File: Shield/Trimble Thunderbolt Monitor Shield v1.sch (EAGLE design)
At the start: 32 parts, among them Q1 2N2222, U2 MAX232PTH

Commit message: Changed the pot used for LCD contrast to a 3362U package.
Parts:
- TRIMLCD: device SparkFun:POTTRIM -> SparkFun:POT100K_3362U
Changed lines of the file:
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@@
 <part name="GND4" library="supply1" deviceset="GND" device=""/>
 <part name="GND5" library="supply1" deviceset="GND" device=""/>
-<part name="TRIMLCD" library="SparkFun" deviceset="POT" device="TRIM" value="10K"/>
+<part name="TRIMLCD" library="SparkFun" deviceset="POT" device="100K_3362U" value="10K"/>
 <part name="R7" library="SparkFun" deviceset="RESISTOR" device="AXIAL-0.3" value="4.7K"/>
 <part name="R8" library="SparkFun" deviceset="RESISTOR" device="AXIAL-0.3" value="10K"/>

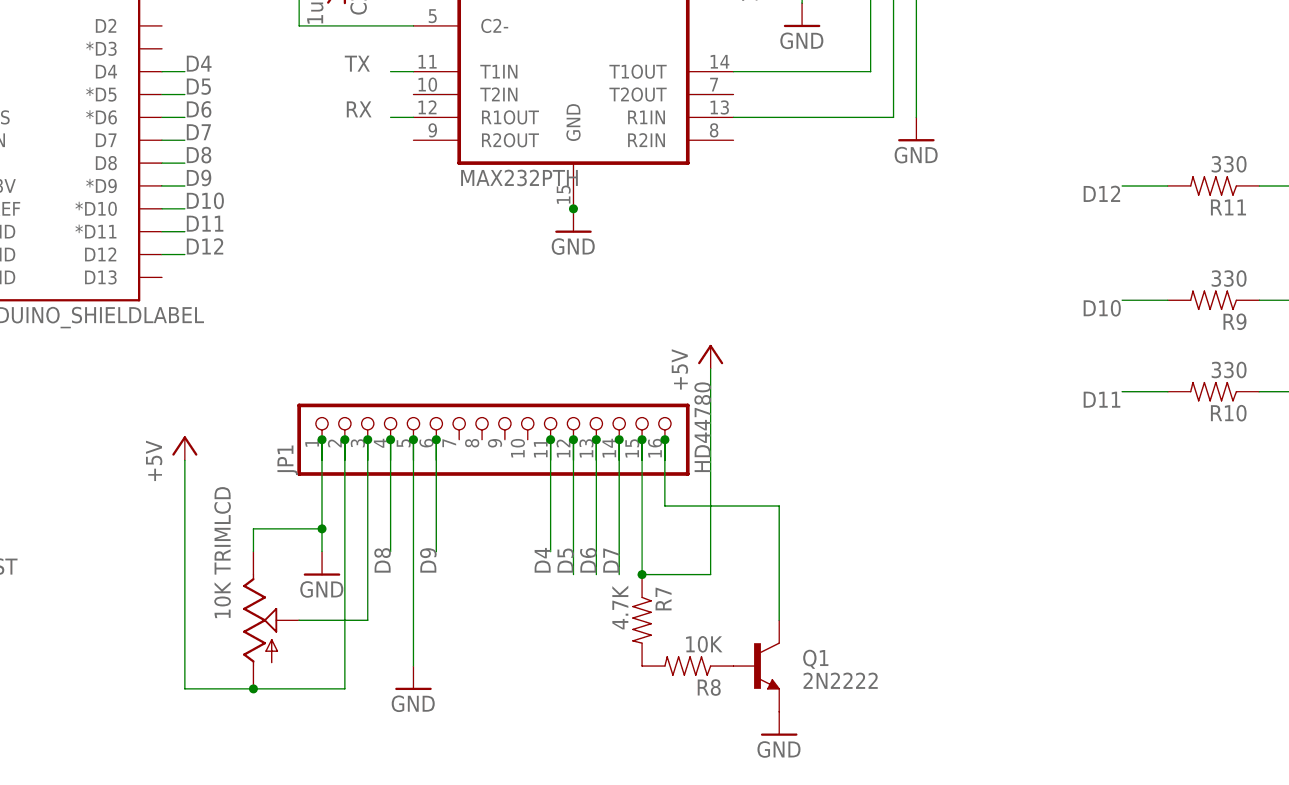
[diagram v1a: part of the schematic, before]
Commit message: Backlight and track routing changes
Changes to the layout of some of the tracks to make them look neater.
Also changed the way the backlight interacts with the Netduino.  It is
now possible to control the brightness of the LCD via a pin on the
Netduino.

Also changed some of the LED output pins
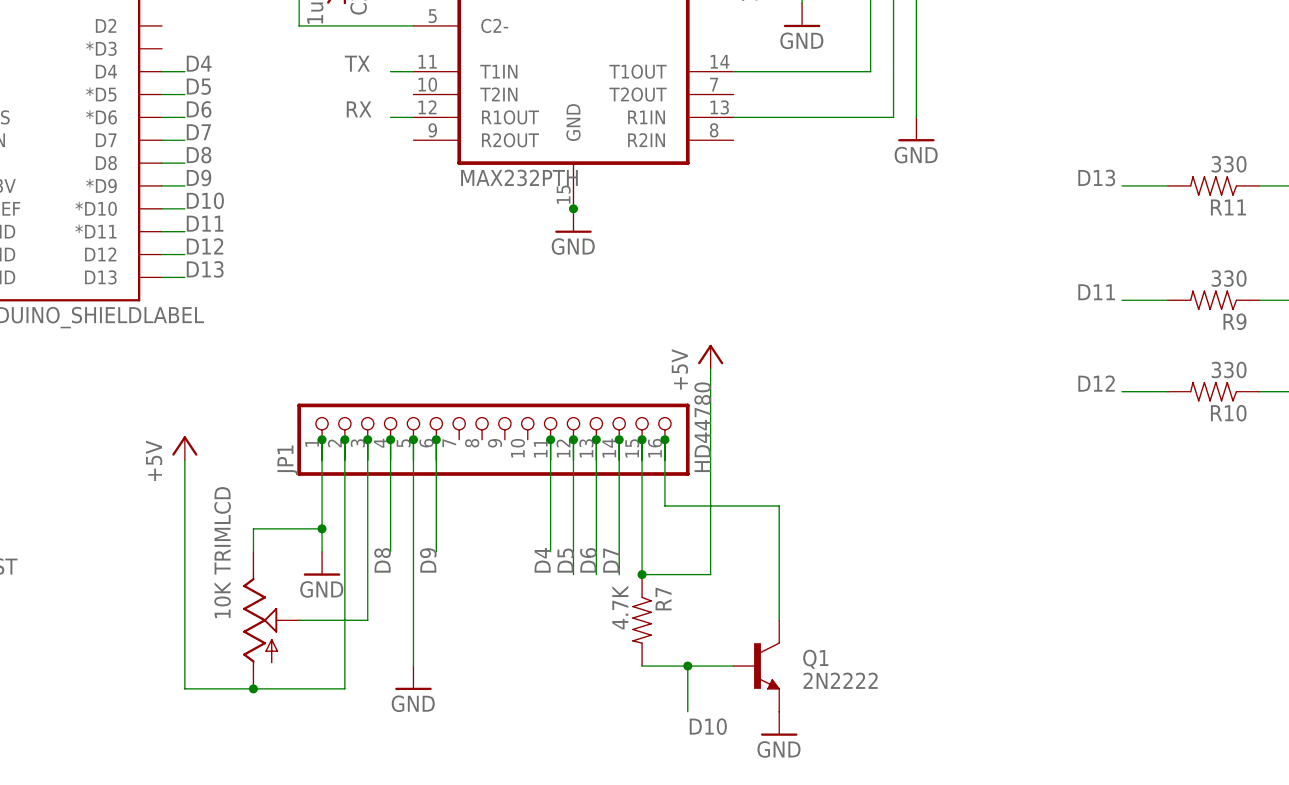
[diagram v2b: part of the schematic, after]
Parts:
- removed R8: 10K, SparkFun:RESISTORAXIAL-0.3
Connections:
- removed net N$11: R7.2, R8.2
- removed net N$12: Q1.B, R8.1
- new net D13: GND.D13, R11.2
- net D10: now also Q1.B, R7.2; no longer R9.2
- net D11: now also R9.2; no longer R10.2
- net D12: now also R10.2; no longer R11.2
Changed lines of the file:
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@@
 <part name="TRIMLCD" library="SparkFun" deviceset="POT" device="100K_3362U" value="10K"/>
 <part name="R7" library="SparkFun" deviceset="RESISTOR" device="AXIAL-0.3" value="4.7K"/>
-<part name="R8" library="SparkFun" deviceset="RESISTOR" device="AXIAL-0.3" value="10K"/>
 <part name="P+3" library="supply1" deviceset="+5V" device=""/>
 <part name="Q1" library="SparkFun" deviceset="TRANSISTOR_NPN" device="TO-92-AMMO" value="2N2222"/>
@@
 </instance>
 <instance part="R7" gate="G$1" x="121.92" y="2.54" rot="R270"/>
-<instance part="R8" gate="G$1" x="127" y="-2.54" rot="R180"/>
 <instance part="P+3" gate="1" x="129.54" y="33.02"/>
 <instance part="Q1" gate="G$1" x="134.62" y="-2.54"/>
@@
 </segment>
 </net>
-<net name="N$11" class="0">
-<segment>
-<pinref part="R7" gate="G$1" pin="2"/>
-<pinref part="R8" gate="G$1" pin="2"/>
-</segment>
-</net>
-<net name="N$12" class="0">
-<segment>
-<pinref part="R8" gate="G$1" pin="1"/>
-<pinref part="Q1" gate="G$1" pin="B"/>
-</segment>
-</net>
 <net name="N$7" class="0">
 <segment>
@@
 </segment>
 <segment>
-<pinref part="R9" gate="G$1" pin="2"/>
-<wire x1="180.34" y1="38.1" x2="175.26" y2="38.1" width="0.1524" layer="91"/>
-<label x="175.26" y="38.1" size="1.778" layer="95" rot="R180"/>
+<pinref part="R7" gate="G$1" pin="2"/>
+<pinref part="Q1" gate="G$1" pin="B"/>
+<wire x1="121.92" y1="-2.54" x2="127" y2="-2.54" width="0.1524" layer="91"/>
+<wire x1="127" y1="-2.54" x2="132.08" y2="-2.54" width="0.1524" layer="91"/>
+<wire x1="127" y1="-2.54" x2="127" y2="-7.62" width="0.1524" layer="91"/>
+<label x="127" y="-10.16" size="1.778" layer="95"/>
+<junction x="127" y="-2.54"/>
 </segment>
 </net>
@@
 </segment>
 <segment>
-<pinref part="R10" gate="G$1" pin="2"/>
-<wire x1="180.34" y1="27.94" x2="175.26" y2="27.94" width="0.1524" layer="91"/>
-<label x="175.26" y="27.94" size="1.778" layer="95" rot="R180"/>
+<pinref part="R9" gate="G$1" pin="2"/>
+<wire x1="180.34" y1="38.1" x2="175.26" y2="38.1" width="0.1524" layer="91"/>
+<label x="170.18" y="38.1" size="1.778" layer="95"/>
 </segment>
 </net>
@@
 </segment>
 <segment>
-<pinref part="R11" gate="G$1" pin="2"/>
-<wire x1="180.34" y1="50.8" x2="175.26" y2="50.8" width="0.1524" layer="91"/>
-<label x="175.26" y="50.8" size="1.778" layer="95" rot="R180"/>
+<pinref part="R10" gate="G$1" pin="2"/>
+<wire x1="180.34" y1="27.94" x2="175.26" y2="27.94" width="0.1524" layer="91"/>
+<label x="170.18" y="27.94" size="1.778" layer="95"/>
 </segment>
 </net>
@@
 </segment>
 </net>
+<net name="D13" class="0">
+<segment>
+<pinref part="GND" gate="G$1" pin="D13"/>
+<wire x1="68.58" y1="40.64" x2="71.12" y2="40.64" width="0.1524" layer="91"/>
+<label x="71.12" y="40.64" size="1.778" layer="95"/>
+</segment>
+<segment>
+<pinref part="R11" gate="G$1" pin="2"/>
+<wire x1="180.34" y1="50.8" x2="175.26" y2="50.8" width="0.1524" layer="91"/>
+<label x="170.18" y="50.8" size="1.778" layer="95"/>
+</segment>
+</net>
